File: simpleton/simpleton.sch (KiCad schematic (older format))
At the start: 37 parts

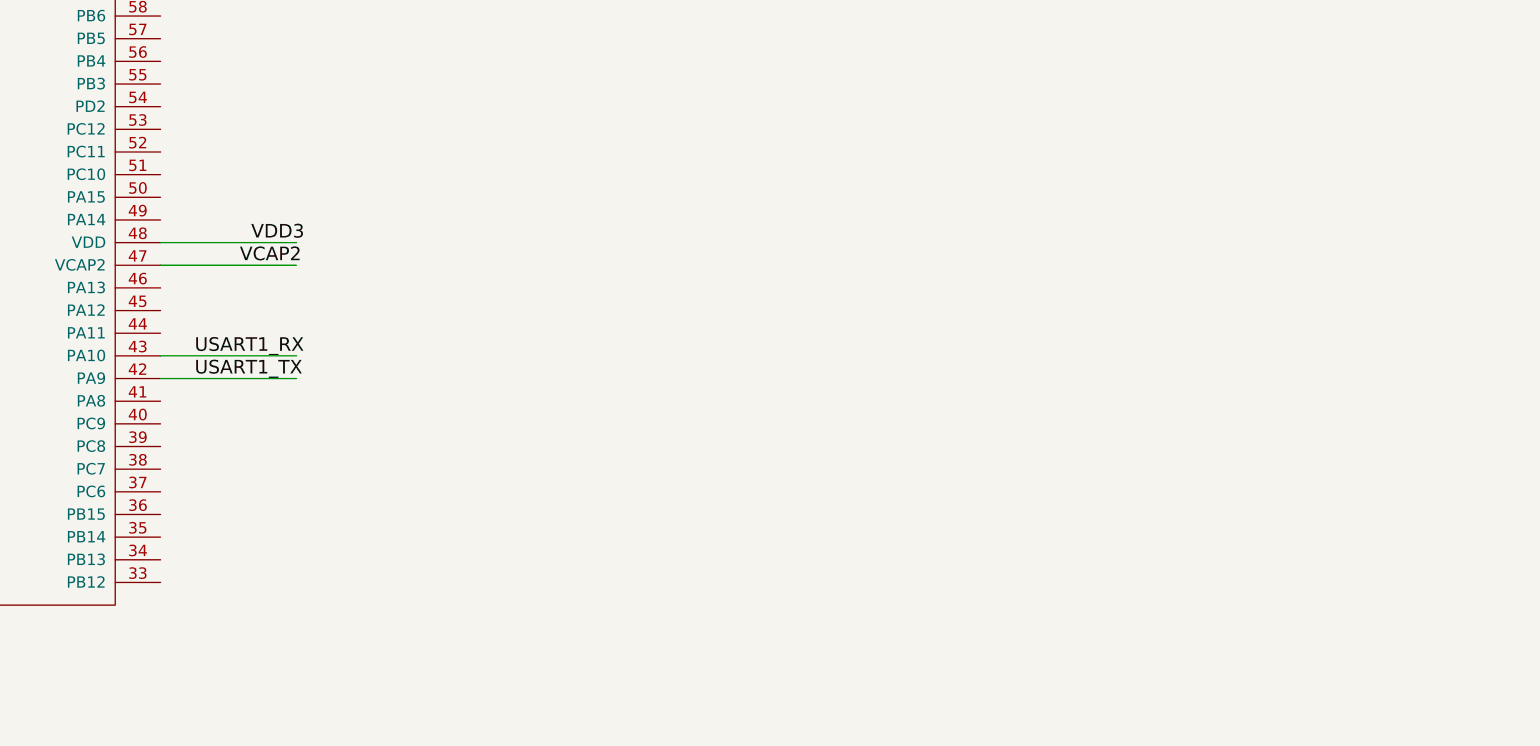
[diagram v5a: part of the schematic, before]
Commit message: Added flash storage
Closes #6

- Added data sheet
- Created N25Q256A33EF840 part
- Connected N25Q256A to power and SPI
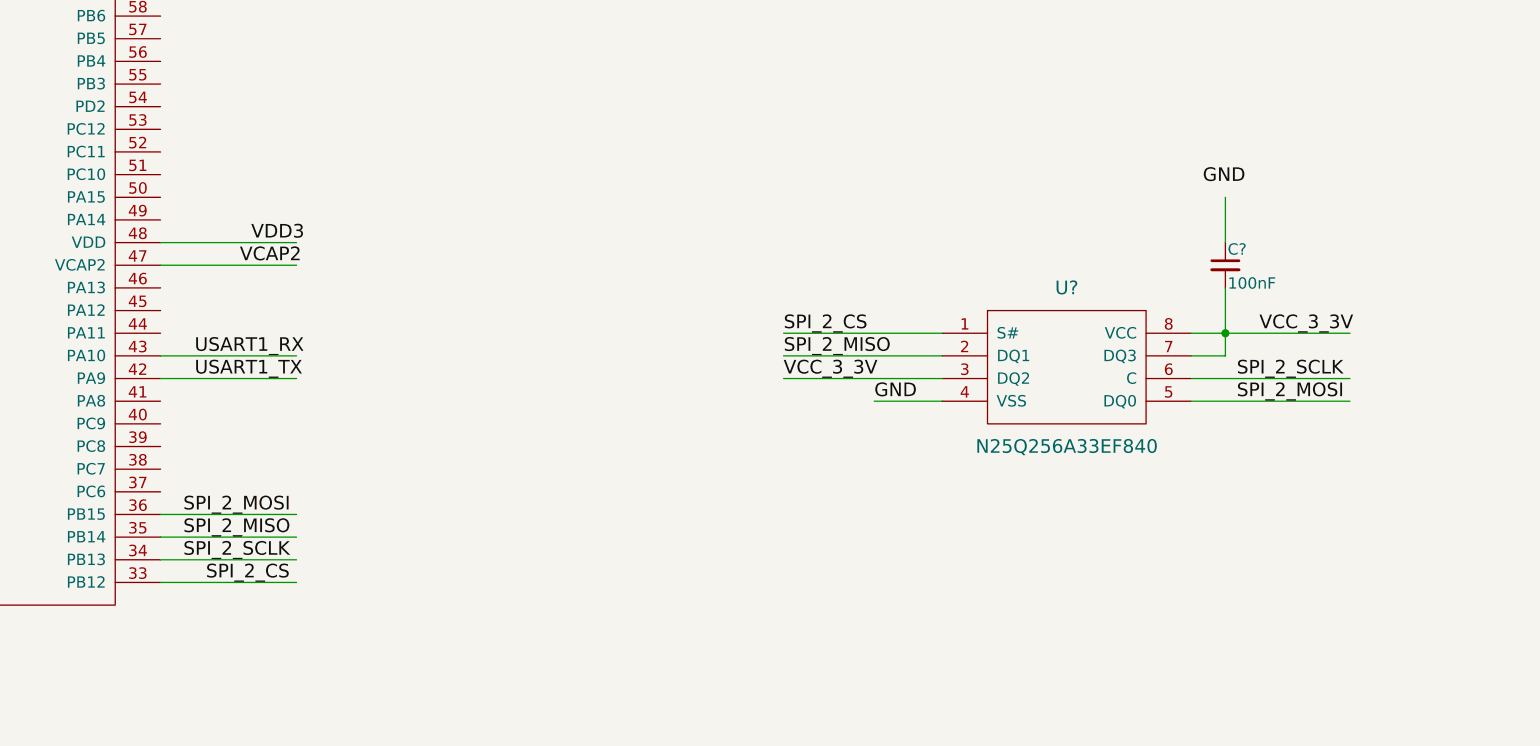
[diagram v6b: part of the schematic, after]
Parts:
- added C?: 100nF, symbol C_Small
- added U?: N25Q256A33EF840, symbol N25Q256A33EF840
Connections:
- net labels added: SPI_2_CS, SPI_2_MISO, SPI_2_MOSI, SPI_2_SCLK
- wire segments 124 -> 138

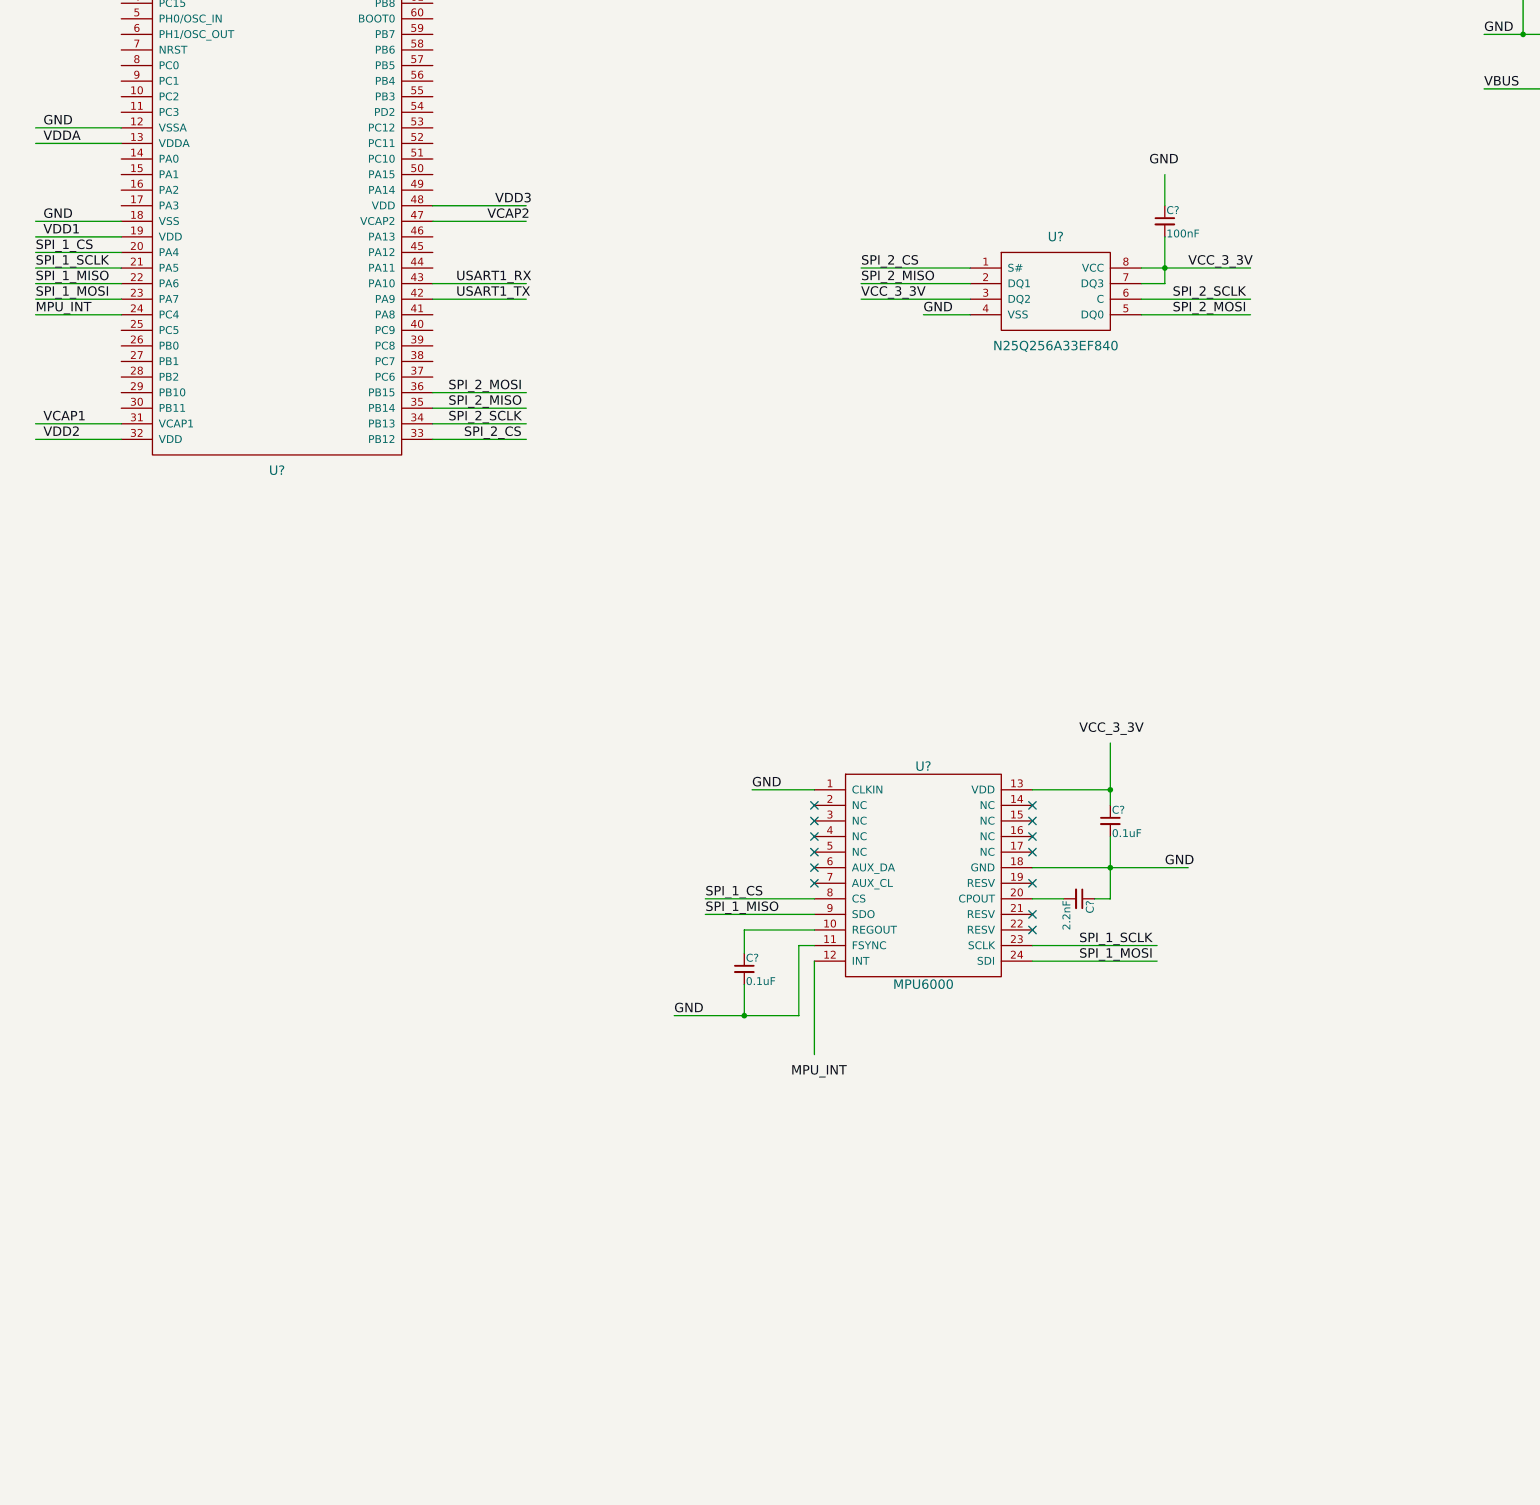
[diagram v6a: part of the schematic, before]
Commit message: Added MAX7456
Closes #7

- Created MAX7456 component
- Connected component to SPI3 and power
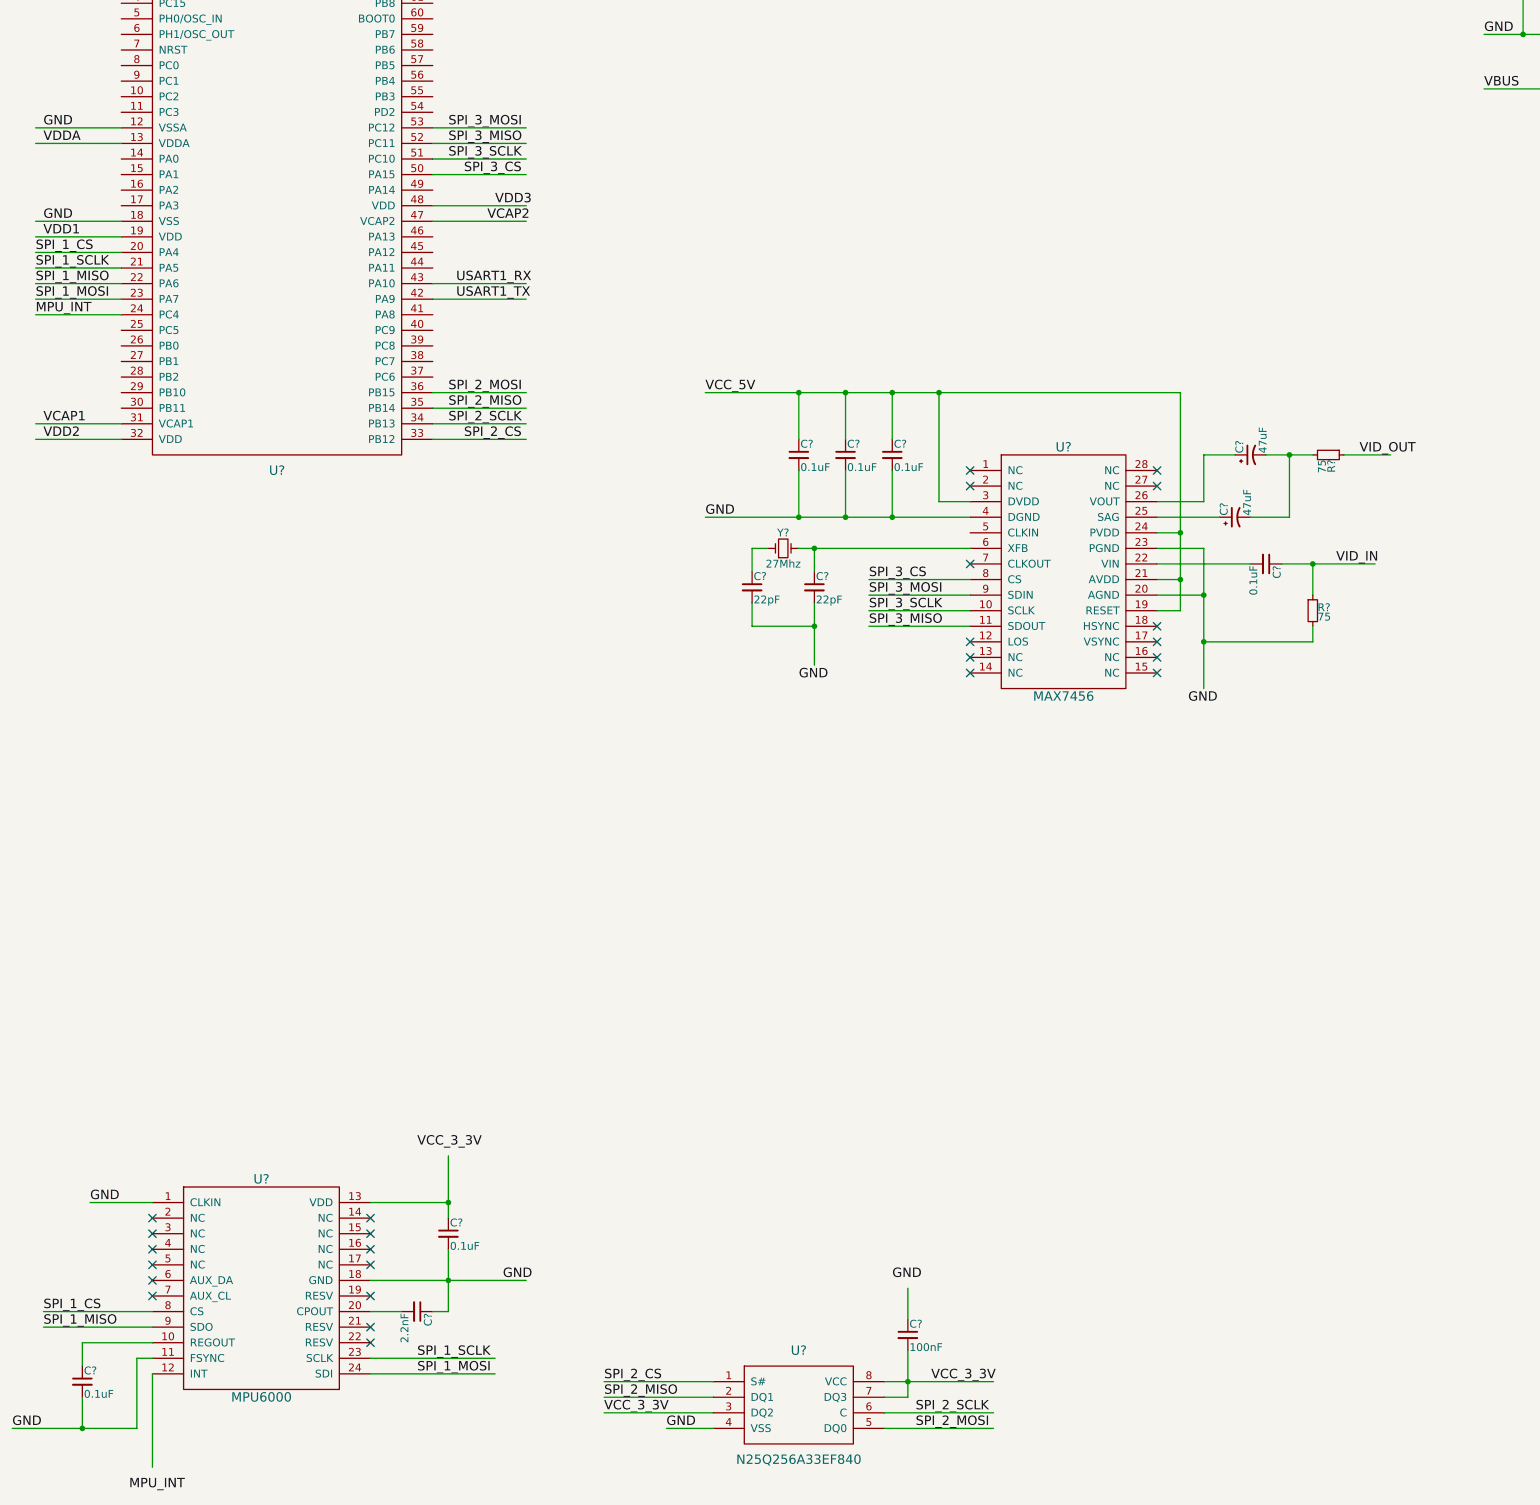
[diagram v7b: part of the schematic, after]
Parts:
- added C? (x4): 0.1uF, symbol C_Small
- added C? (x2): 22pF, symbol C_Small
- added C? (x2): 47uF, symbol CP1_Small
- added R? (x2): 75, symbol R_Small
- added U?: MAX7456, symbol MAX7456
- added Y?: 27Mhz, symbol Crystal_Small
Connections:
- net labels added: SPI_3_CS, SPI_3_MISO, SPI_3_MOSI, SPI_3_SCLK, VID_IN, VID_OUT
- wire segments 138 -> 183
- no-connect marks 27 -> 39
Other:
- moved on the sheet: C?, U?
